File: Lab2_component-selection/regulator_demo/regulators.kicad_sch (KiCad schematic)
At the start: 23 parts, among them J1 n.m., J2 n.m., J3 n.m., J4 n.m., U1 LM317_SOT-223, U2 TPS79301-EP, U3 MIC5366-3.3YC5

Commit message: updated schematic
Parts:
- R1: value R -> UNKNOWN1
- R2: value R -> UNKNOWN2
- R3: value R -> UNKNOWN4
- R4: value R -> UNKNOWN5
- R5: value R -> UNKNOWN7
- R6: value R -> UNKNOWN8
- R7: value R -> UNKNOWN3
- R8: value R -> UNKNOWN6
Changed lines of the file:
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@@
       (effects (font (size 1.27 1.27)) (justify left))
     )
-    (property "Value" "R" (at 180.34 62.865 0)
+    (property "Value" "UNKNOWN7" (at 180.34 62.865 0)
       (effects (font (size 1.27 1.27)) (justify left))
     )
@@
   (symbol (lib_id "Device:R") (at 56.515 66.04 90) (unit 1)
     (in_bom yes) (on_board yes) (dnp no) (fields_autoplaced)
-    (property "Reference" "R2" (at 56.515 60.325 90)
-      (effects (font (size 1.27 1.27)))
-    )
-    (property "Value" "R" (at 56.515 62.865 90)
+    (property "Reference" "R2" (at 56.515 59.69 90)
+      (effects (font (size 1.27 1.27)))
+    )
+    (property "Value" "UNKNOWN2" (at 56.515 62.23 90)
       (effects (font (size 1.27 1.27)))
     )
@@
       (effects (font (size 1.27 1.27)) (justify left))
     )
-    (property "Value" "R" (at 180.34 73.025 0)
+    (property "Value" "UNKNOWN8" (at 180.34 73.025 0)
       (effects (font (size 1.27 1.27)) (justify left))
     )
@@
       (effects (font (size 1.27 1.27)) (justify left))
     )
-    (property "Value" "R" (at 77.47 72.39 0)
+    (property "Value" "UNKNOWN3" (at 77.47 72.39 0)
       (effects (font (size 1.27 1.27)) (justify left))
     )
@@
   (symbol (lib_id "Device:R") (at 64.135 123.825 0) (unit 1)
     (in_bom yes) (on_board yes) (dnp no) (fields_autoplaced)
-    (property "Reference" "R4" (at 66.675 122.555 0)
-      (effects (font (size 1.27 1.27)) (justify left))
-    )
-    (property "Value" "R" (at 66.675 125.095 0)
+    (property "Reference" "R4" (at 66.04 122.555 0)
+      (effects (font (size 1.27 1.27)) (justify left))
+    )
+    (property "Value" "UNKNOWN5" (at 66.04 125.095 0)
       (effects (font (size 1.27 1.27)) (justify left))
     )
@@
   (symbol (lib_id "Device:R") (at 84.455 123.19 0) (unit 1)
     (in_bom yes) (on_board yes) (dnp no) (fields_autoplaced)
-    (property "Reference" "R8" (at 86.995 121.92 0)
-      (effects (font (size 1.27 1.27)) (justify left))
-    )
-    (property "Value" "R" (at 86.995 124.46 0)
+    (property "Reference" "R8" (at 86.36 121.92 0)
+      (effects (font (size 1.27 1.27)) (justify left))
+    )
+    (property "Value" "UNKNOWN6" (at 86.36 124.46 0)
       (effects (font (size 1.27 1.27)) (justify left))
     )
@@
   (symbol (lib_id "Device:R") (at 64.135 111.76 0) (unit 1)
     (in_bom yes) (on_board yes) (dnp no) (fields_autoplaced)
-    (property "Reference" "R3" (at 66.675 110.49 0)
-      (effects (font (size 1.27 1.27)) (justify left))
-    )
-    (property "Value" "R" (at 66.675 113.03 0)
+    (property "Reference" "R3" (at 66.04 110.49 0)
+      (effects (font (size 1.27 1.27)) (justify left))
+    )
+    (property "Value" "UNKNOWN4" (at 66.04 113.03 0)
       (effects (font (size 1.27 1.27)) (justify left))
     )
@@
   (symbol (lib_id "Device:R") (at 48.895 71.755 0) (unit 1)
     (in_bom yes) (on_board yes) (dnp no) (fields_autoplaced)
-    (property "Reference" "R1" (at 51.435 70.485 0)
-      (effects (font (size 1.27 1.27)) (justify left))
-    )
-    (property "Value" "R" (at 51.435 73.025 0)
-      (effects (font (size 1.27 1.27)) (justify left))
-    )
+    (property "Reference" "R1" (at 50.8 70.485 0)
+      (effects (font (size 1.27 1.27)) (justify left))
+    )
+    (property "Value" "UNKNOWN1" (at 50.8 73.025 0)
+      (effects (font (size 1.27 1.27)) (justify left))
+    )

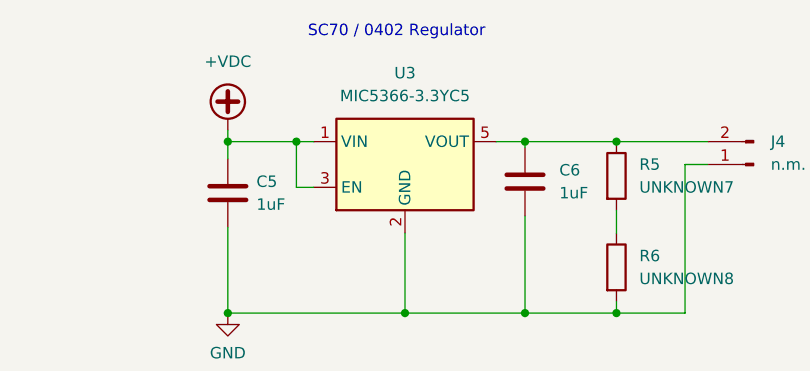
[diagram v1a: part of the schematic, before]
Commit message: updated part number on regulator
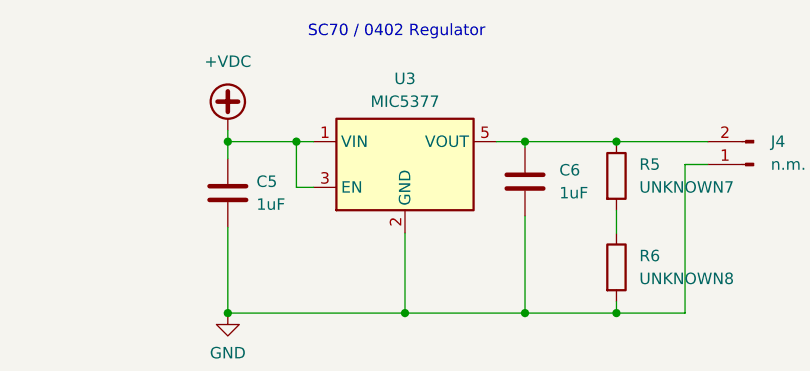
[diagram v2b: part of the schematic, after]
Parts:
- U3: value MIC5366-3.3YC5 -> MIC5377
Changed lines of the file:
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@@
   (symbol (lib_id "Regulator_Linear:MIC5366-3.3YC5") (at 154.305 60.325 0) (unit 1)
     (in_bom yes) (on_board yes) (dnp no) (fields_autoplaced)
-    (property "Reference" "U3" (at 154.305 50.165 0)
+    (property "Reference" "U3" (at 154.305 50.8 0)
       (effects (font (size 1.27 1.27)))
     )
-    (property "Value" "MIC5366-3.3YC5" (at 154.305 52.705 0)
+    (property "Value" "MIC5377" (at 154.305 53.34 0)
       (effects (font (size 1.27 1.27)))
     )
